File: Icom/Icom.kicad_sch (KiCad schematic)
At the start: 5 parts, among them J1 OHIS RJ45, J2 Icom RJ45 Mic, J3 Icom GX16-8P Mic, J4 Headphone In

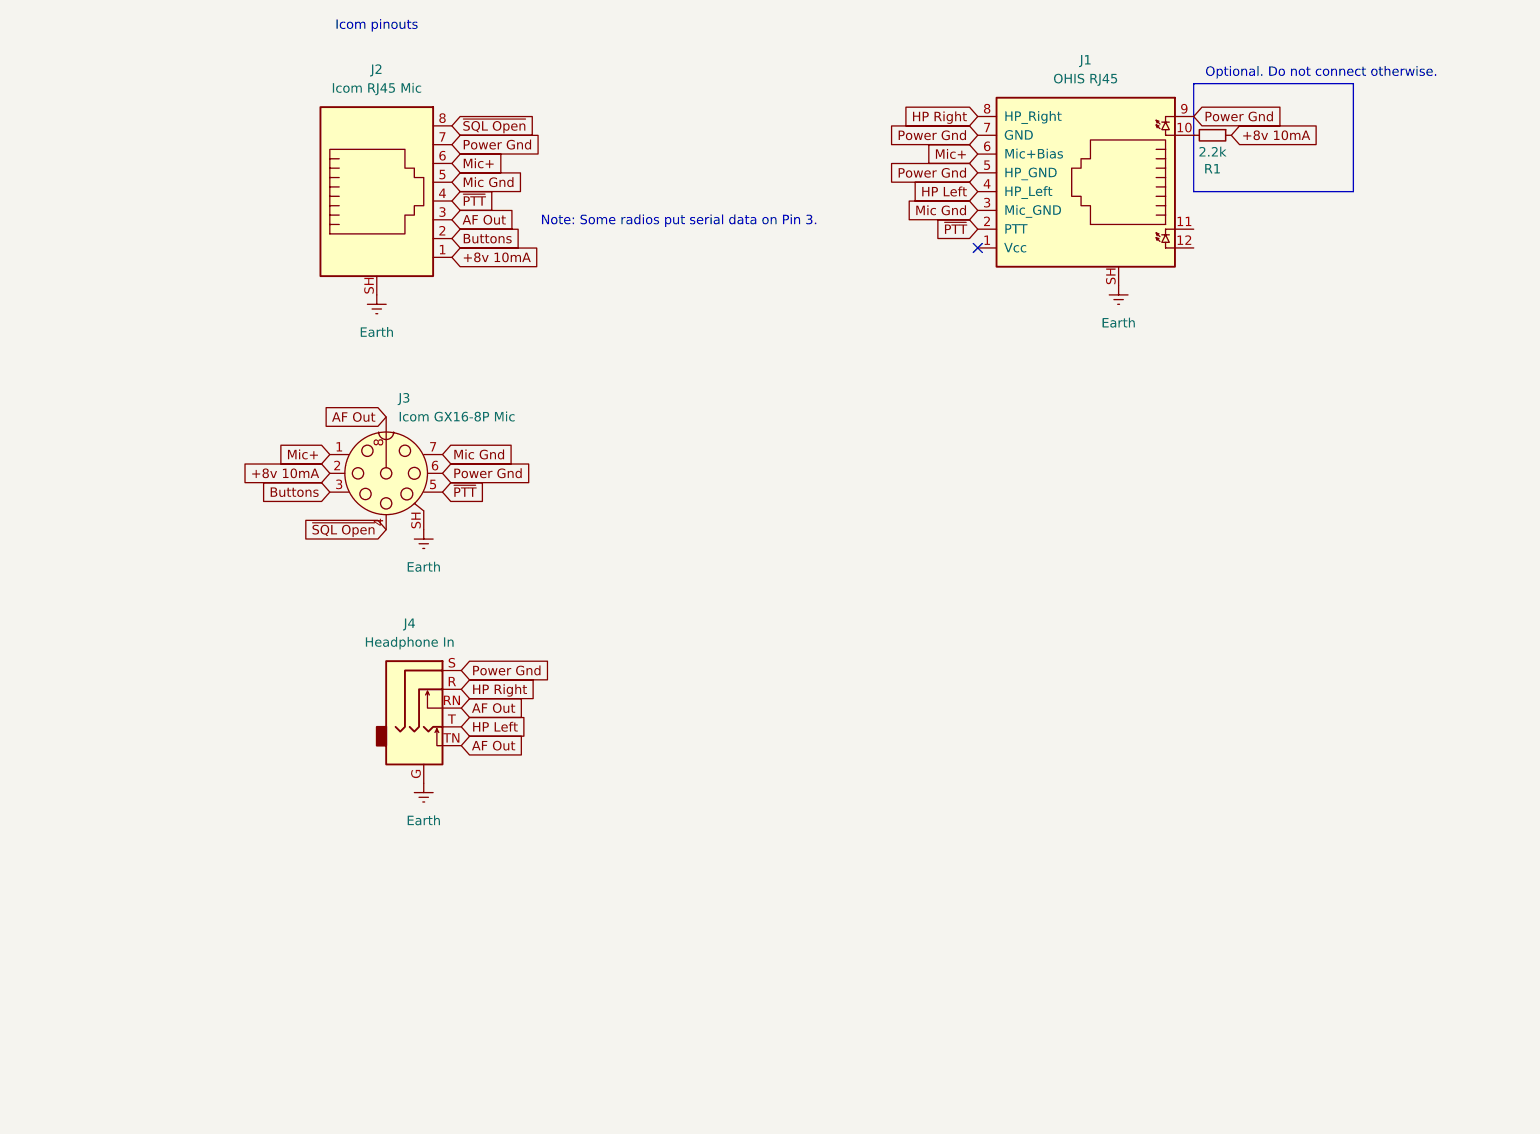
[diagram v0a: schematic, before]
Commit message: Icom pinout references. Renamed Earth to Shield.
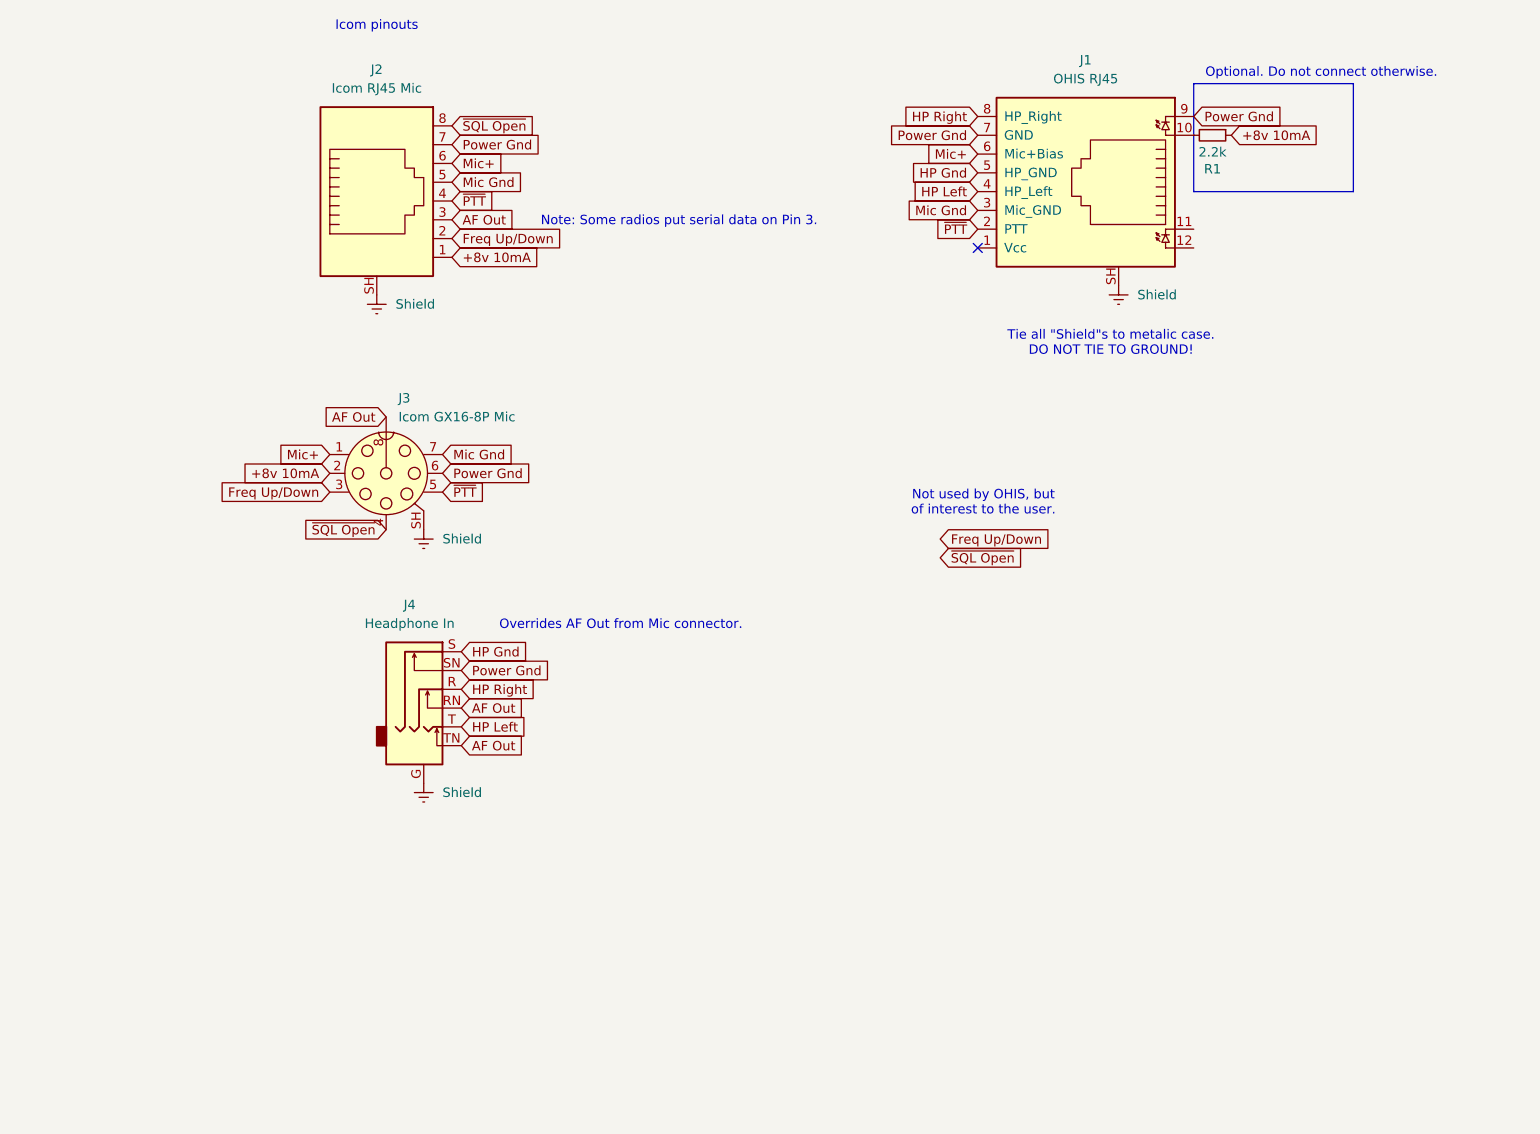
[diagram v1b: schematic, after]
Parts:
- removed J4: Headphone In, symbol Connector_Audio:AudioJack3_Ground_SwitchTR
- added J4: Headphone In, symbol Connector_Audio:AudioJack3_Ground_Switch
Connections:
- net AF Out: now also J4.RN, J4.TN
- net HP Left: now also J4.T
- net HP Right: now also J4.R
- net Power Gnd: now also J4.SN; no longer J1.5 (HP_GND)
- net Buttons renamed Freq Up/Down
- net Earth renamed Shield
- net Shield: now also J4.G
- new net HP Gnd: J1.5 (HP_GND), J4.S
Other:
- note added: "Not used by OHIS, but of interest to the user."
- note added: "Overrides AF Out from Mic connector."
- note added: "Tie all "Shield"s to metalic case. DO NOT TIE TO GROUND!"

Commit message: See #1, for Icom. Not happy with this, but committing for record.
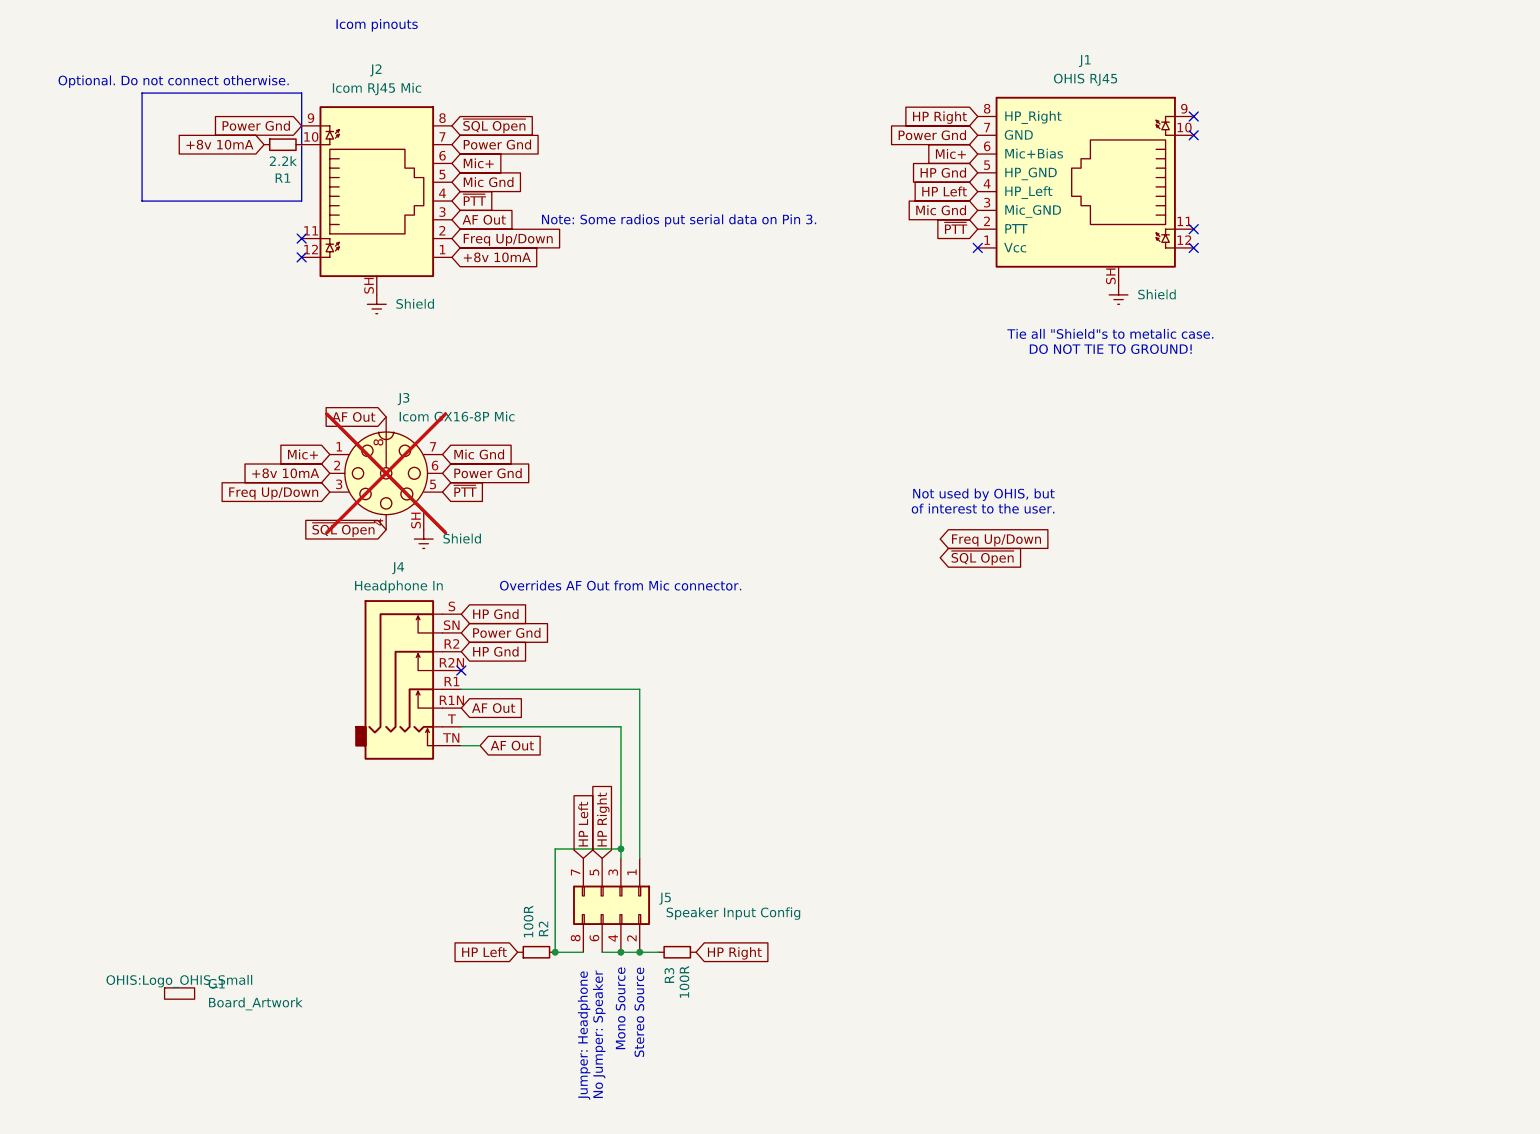
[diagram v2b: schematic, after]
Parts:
- added G1: Board_Artwork, OHIS:Logo_OHIS_Small, symbol Smitty:Board_Artwork
- added J5: Speaker Input Config, Connector_PinHeader_2.54mm:PinHeader_2x04_P2.54mm_Horizontal, symbol Connector_Generic:Conn_02x04_Odd_Even
- added R2, R3: 100R, Resistor_SMD:R_0603_1608Metric, symbol Device:R_Small
- J1: footprint (none) -> Connector_RJ:RJ45_Amphenol_RJHSE538X; LCSC (none) -> C138392
- J2: footprint (none) -> Connector_RJ:RJ45_Amphenol_RJHSE538X; symbol Connector:RJ45_Shielded -> Connector:RJ45_LED_Shielded; LCSC (none) -> C138392
- J3: now not fitted; now left out of the parts list
- J4: footprint (none) -> Libraries:Conn_3.5mm-PJ-393_C2837065_C668609_C128990; symbol Connector_Audio:AudioJack3_Ground_Switch -> Smitty:AudioJack4_SwitchTR1R2S; LCSC (none) -> C2939584
- R1: footprint (none) -> Resistor_SMD:R_0603_1608Metric; LCSC (none) -> C4190
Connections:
- net AF Out: now also J4.R1N; no longer J4.RN
- net HP Gnd: now also J4.R2
- net HP Left: now also J5.7 (Pin_7), R2.1; no longer J4.T
- net HP Right: now also J5.5 (Pin_5), R3.1; no longer J4.R
- net Power Gnd: now also J2.9; no longer J1.9
- net Shield: no longer J4.G
- net at R1.2: now also J2.10; no longer J1.10
- new net: J4.R1, J5.1 (Pin_1)
- new net: J5.2 (Pin_2), J5.4 (Pin_4), J5.6 (Pin_6), R3.2
- new net: J4.T, J5.3 (Pin_3), J5.8 (Pin_8), R2.2
- no-connect marks 1 -> 8
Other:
- note added: "Jumper: Headphone No Jumper: Speaker"
- note added: "Mono Source"
- note added: "Stereo Source"
- moved on the sheet: R1

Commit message: For #1. Looks much more like the User Adapter.
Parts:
- added H1, H2, H3: MountingHole_Pad, MountingHole:MountingHole_3.2mm_M3_Pad, symbol Mechanical:MountingHole_Pad
- added R4, R5: 100R, Resistor_THT:R_Axial_DIN0207_L6.3mm_D2.5mm_P7.62mm_Horizontal, symbol Device:R_Small
- added R6: 2.2k, Resistor_THT:R_Axial_DIN0207_L6.3mm_D2.5mm_P7.62mm_Horizontal, symbol Device:R_Small
- J4: footprint Libraries:Conn_3.5mm-PJ-393_C2837065_C668609_C128990 -> Libraries:Conn_3.5mm-PJ-393_SMT-C668609_TH-C145811; LCSC C2939584 -> C6688609
- R1: footprint Resistor_SMD:R_0603_1608Metric -> Resistor_SMD:R_1206_3216Metric; LCSC C4190 -> (none)
- R2, R3: footprint Resistor_SMD:R_0603_1608Metric -> Resistor_SMD:R_1206_3216Metric; LCSC C22775 -> (none)
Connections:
- net +8v 10mA: now also R6.1
- net HP Left: now also R4.1
- net HP Right: now also R5.2
- net Shield: now also H1.1, H2.1, H3.1
- net at J2.10, R1.2: now also R6.2
- net at J5.2 (Pin_2), J5.4 (Pin_4), J5.6 (Pin_6)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: now also R5.1
- net at J4.T, J5.3 (Pin_3), J5.8 (Pin_8)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: now also R4.2
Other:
- moved on the sheet: R1

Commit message: Kenwood laid out more similarly to the User Adapter. #1
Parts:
- added H4: MountingHole_Pad, MountingHole:MountingHole_3.2mm_M3_Pad, symbol Mechanical:MountingHole_Pad
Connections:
- net Shield: now also H4.1
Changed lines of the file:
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@@
+	)
+	(symbol
+		(lib_id "power:Earth")
+		(at 212.09 105.41 0)
+		(unit 1)
+		(exclude_from_sim no)
+		(in_bom yes)
+		(on_board yes)
+		(dnp no)
+		(fields_autoplaced yes)
+		(property "Reference" "#PWR07"
+			(at 212.09 111.76 0)
+			(effects
+				(font
+					(size 1.27 1.27)
+				)
+				(hide yes)
+			)
+		)
+		(property "Value" "Shield"
+			(at 214.63 106.6799 0)
+			(effects
+				(font
+					(size 1.27 1.27)
+				)
+				(justify left)
+			)
+		)
+		(property "Footprint" ""
+			(at 212.09 105.41 0)
+			(effects
+				(font
+					(size 1.27 1.27)
+				)
+				(hide yes)
+			)
+		)
+		(property "Datasheet" "~"
+			(at 212.09 105.41 0)
+			(effects
+				(font
+					(size 1.27 1.27)
+				)
+				(hide yes)
+			)
+		)
+		(property "Description" "Power symbol creates a global label with name \"Earth\""
+			(at 212.09 105.41 0)
+			(effects
+				(font
+					(size 1.27 1.27)
+				)
+				(hide yes)
+			)
+		)
+		(pin "1"
+		)
+		(instances
+			(project "Icom"
+				(path "/6a3924fa-c381-477c-bc5e-4effe098c460"
+					(reference "#PWR07")
+					(unit 1)
+				)
+			)
+		)
 	)
 	(symbol
@@
 					(unit 1)
 				)
+			)
+		)
+	)
+	(symbol
+		(lib_id "Mechanical:MountingHole_Pad")
+		(at 212.09 102.87 0)
+		(unit 1)
+		(exclude_from_sim yes)
+		(in_bom no)
+		(on_board yes)
+		(dnp no)
+		(fields_autoplaced yes)
+		(property "Reference" "H4"
+			(at 214.63 100.3299 0)
+			(effects
+				(font
+					(size 1.27 1.27)
+				)
+				(justify left)
+			)
+		)
+		(property "Value" "MountingHole_Pad"
+			(at 214.63 102.8699 0)
+			(effects
+				(font
+					(size 1.27 1.27)
+				)
+				(justify left)
+			)
+		)
+		(property "Footprint" "MountingHole:MountingHole_3.2mm_M3_Pad"
+			(at 212.09 102.87 0)
+			(effects
+				(font
+					(size 1.27 1.27)
+				)
+				(hide yes)
+			)
+		)
+		(property "Datasheet" "~"
+			(at 212.09 102.87 0)
+			(effects
+				(font
+					(size 1.27 1.27)
+				)
+				(hide yes)
+			)
+		)
+		(property "Description" "Mounting Hole with connection"
+			(at 212.09 102.87 0)
+			(effects
+				(font
+					(size 1.27 1.27)
+				)
+				(hide yes)
+			)
+		)
+		(pin "1"
+		)
+		(instances
+			(project "Icom"
+				(path "/6a3924fa-c381-477c-bc5e-4effe098c460"
+					(reference "H4")
+					(unit 1)
+				)
